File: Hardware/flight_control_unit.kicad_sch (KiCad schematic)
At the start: 43 parts, among them U15 TDD01H0SB1R, U16 TDD01H0SB1R, U7 STM32F405RGT6, Y2 25MHz

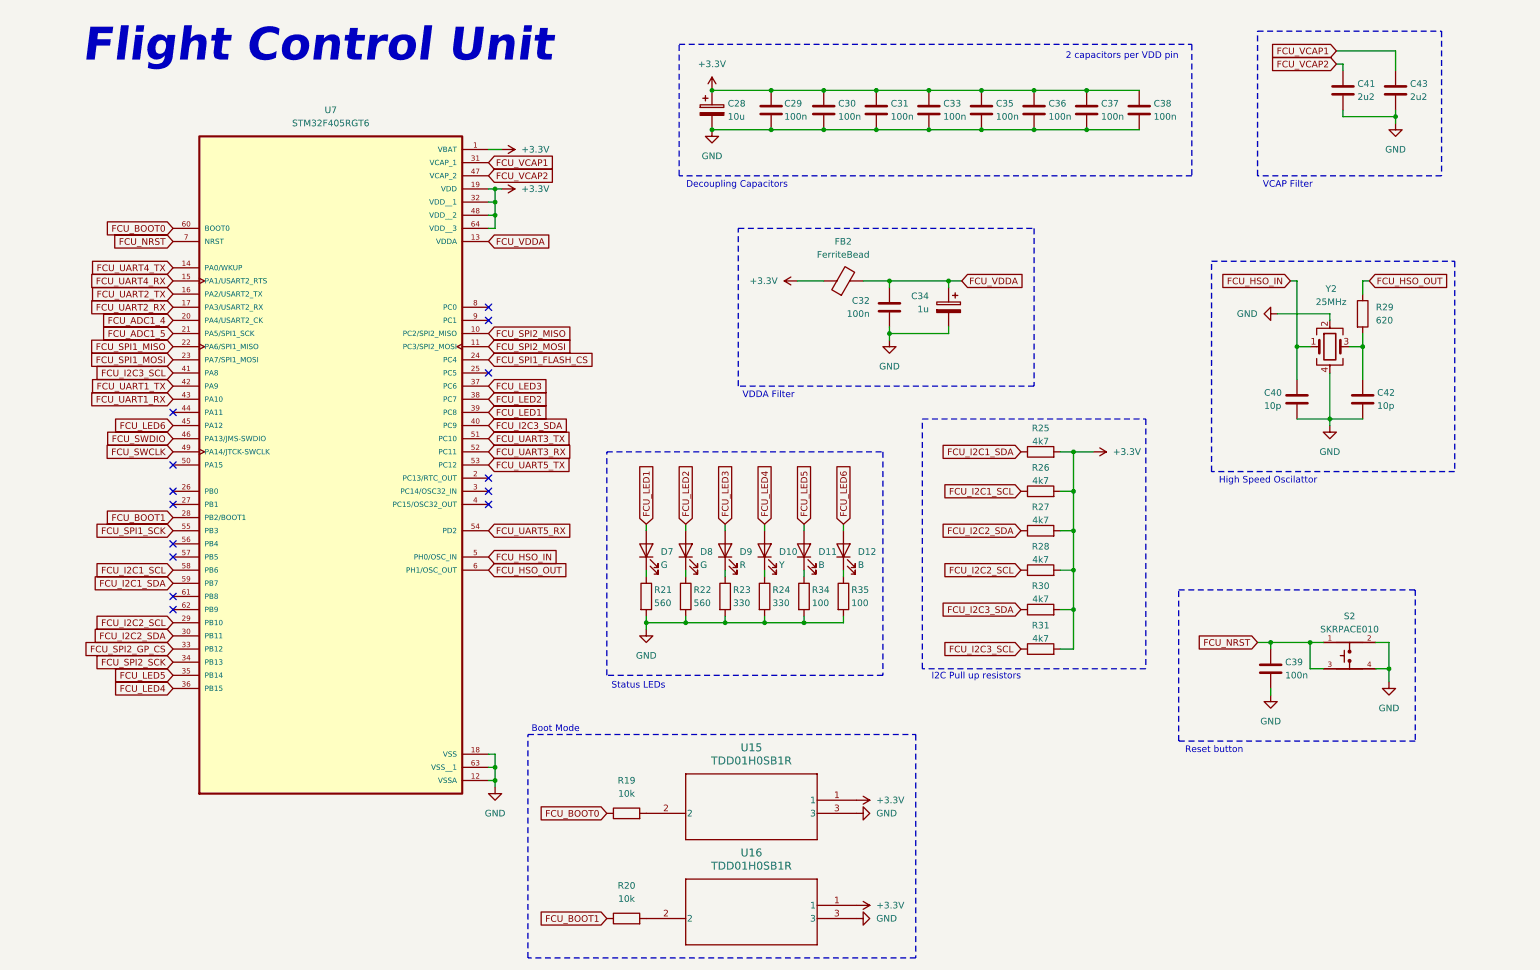
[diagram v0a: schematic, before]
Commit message: fcu, nu schematics, problem with pins
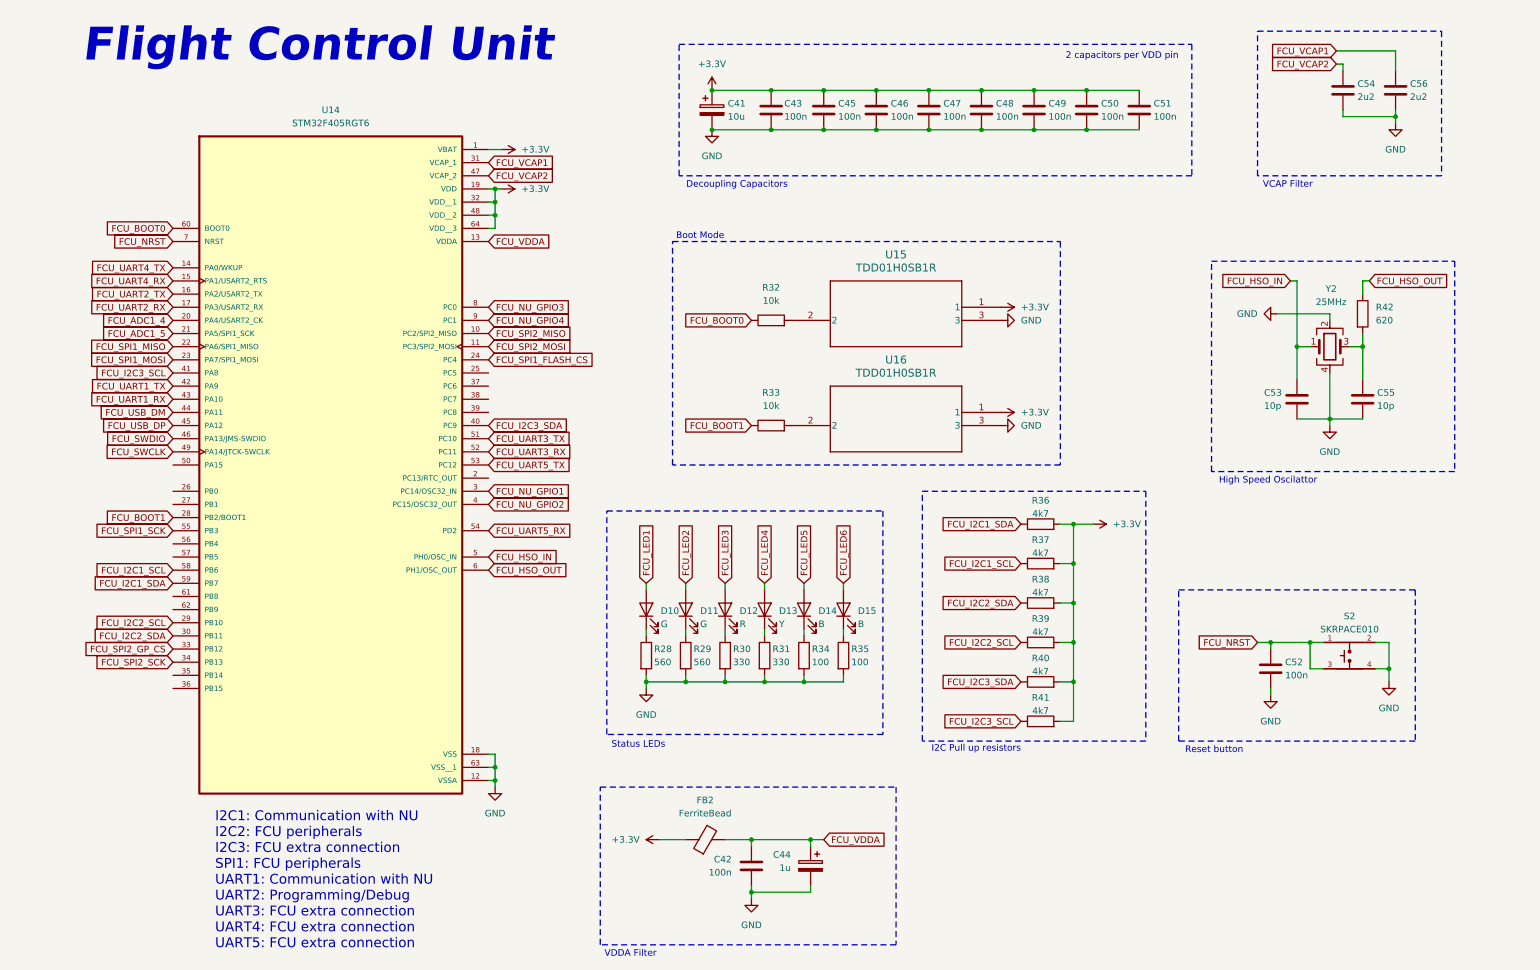
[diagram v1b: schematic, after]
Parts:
- renumbered C28 to C41, C32 to C42, C29 to C43, C34 to C44, C30 to C45, C31 to C46, C33 to C47, C35 to C48, C36 to C49, C37 to C50, C38 to C51, C39 to C52, C40 to C53, C41 to C54, C42 to C55, C43 to C56, D7 to D10, D8 to D11, D9 to D12, D10 to D13, D11 to D14, D12 to D15, R21 to R28, R22 to R29, R23 to R30, R24 to R31, R19 to R32, R20 to R33, R25 to R36, R26 to R37, R27 to R38, R28 to R39, R30 to R40, R31 to R41, R29 to R42, U7 to U14
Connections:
- net FCU_LED1: no longer U14.39 (PC8)
- net FCU_LED2: no longer U14.38 (PC7)
- net FCU_LED3: no longer U14.37 (PC6)
- net FCU_LED4: no longer U14.36 (PB15)
- net FCU_LED5: no longer U14.35 (PB14)
- net FCU_LED6: no longer U14.45 (PA12)
- net FCU_NU_GPIO1: now reaches U14.3 (PC14/OSC32_IN)
- net FCU_NU_GPIO2: now reaches U14.4 (PC15/OSC32_OUT)
- net FCU_USB_DM: now reaches U14.44 (PA11)
- net FCU_NU_GPIO3: now reaches U14.8 (PC0)
- net FCU_NU_GPIO4: now reaches U14.9 (PC1)
- new net FCU_USB_DP: U14.45 (PA12)
- no-connect marks 14 -> 0
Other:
- note added: "I2C1: Communication with NU I2C2: FCU peripherals I2C3: FCU extra connection SPI1: FCU peripherals UART1: Communication with NU UART2: Programming/Debug UART3: FCU extra connection UART4: FCU extra connection UART5: FCU extra connection"
- title: Flight Control Unit - Peripherals -> Flight Control Unit
- moved on the sheet: C42, C44, D10, D11, D12, D13, D14, D15, FB2, R28, R29, R30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

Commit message: pin mess up win, starting over again
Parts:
- removed C41: 10u, symbol Device:C_Polarized
- removed C42, C43, C45, C46, C47, C48, C49, C50, C51, C52: 100n, symbol Device:C
- removed C44: 1u, symbol Device:C_Polarized
- removed C53, C55: 10p, symbol Device:C
- removed C54, C56: 2u2, symbol Device:C
- removed D10, D11: G, symbol Device:LED
- removed D12: R, symbol Device:LED
- removed D13: Y, symbol Device:LED
- removed D14, D15: B, symbol Device:LED
- removed FB2: FerriteBead, symbol Device:FerriteBead
- removed R28, R29: 560, symbol Device:R
- removed R30, R31: 330, symbol Device:R
- removed R32, R33: 10k, symbol Device:R
- removed R34, R35: 100, symbol Device:R
- removed R36, R37, R38, R39, R40, R41: 4k7, symbol Device:R
- removed R42: 620, symbol Device:R
- removed S2: SKRPACE010, SKRPACE010:SW_SKRPACE010, symbol Aircraft_Components:SKRPACE010
- removed U14: STM32F405RGT6, STM32F405RGT6:QFP50P1200X1200X160-64N, symbol Aircraft_Components:STM32F405RGT6
- removed U15, U16: TDD01H0SB1R, SOT_TDDSB1R_CNK, symbol Aircraft_Components:TDD01H0SB1R
- removed Y2: 25MHz, symbol Device:Crystal_GND24
- added C12, C13: 2u2, symbol Device:C
- added C14: 10u, symbol Device:C_Polarized
- added C15, C16, C17, C18, C19, C20, C22, C25, C26: 100n, symbol Device:C
- added C21: 1u, symbol Device:C_Polarized
- added C23, C24: 10p, symbol Device:C
- added D4: R, symbol Device:LED
- added D5: G, symbol Device:LED
- added D6: Y, symbol Device:LED
- added D7: B, symbol Device:LED
- added FB1: FerriteBead, symbol Device:FerriteBead
- added R10: 10k, symbol Device:R
- added R11, R12, R13, R14, R15, R16: 4k7, symbol Device:R
- added R17, R18, R19: 330, symbol Device:R
- added R20: 560, symbol Device:R
- added R9: 620, symbol Device:R
- added SW1: SW_Push_Dual, symbol Switch:SW_Push_Dual
- added SW2: SW_SPDT, symbol Switch:SW_SPDT
- added U14: STM32F405RGTx, Package_QFP:LQFP-64_10x10mm_P0.5mm, symbol MCU_ST_STM32F4:STM32F405RGTx
- added Y1: 25MHz, symbol Device:Crystal_GND24
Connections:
- net +3.3V: now also C14.1, C15.1, C16.1, C17.1, C18.1, C19.1, C25.1, C26.1, FB1.1, R11.1, R12.1, R13.1, R14.1, R15.1, R16.1, SW2.1 (A), U14.1 (VBAT), U14.19 (VDD), U14.32 (VDD), U14.48 (VDD), U14.64 (VDD)
- net FCU_BOOT0: now also R10.1, U14.60 (BOOT0)
- net FCU_I2C1_SCL: now also R11.2, U14.61 (PB8)
- net FCU_I2C1_SDA: now also R12.2, U14.59 (PB7)
- net FCU_I2C2_SCL: now also R13.2, U14.29 (PB10)
- net FCU_I2C2_SDA: now also R14.2, U14.30 (PB11)
- net FCU_I2C3_SCL: now also R15.2, U14.41 (PA8)
- net FCU_I2C3_SDA: now also R16.2, U14.40 (PC9)
- net FCU_LED1: now also D7.2 (A), U14.8 (PC0)
- net FCU_LED2: now also D6.2 (A), U14.9 (PC1)
- net FCU_LED3: now also D5.2 (A), U14.10 (PC2)
- net FCU_LED4: now also D4.2 (A), U14.11 (PC3)
- net FCU_NRST: now also C22.1, SW1.2, SW1.4, U14.7 (NRST)
- net FCU_SPI1_MISO: now also U14.22 (PA6)
- net FCU_SPI1_MOSI: now also U14.23 (PA7)
- net FCU_SWCLK: now also U14.49 (PA14)
- net FCU_SWDIO: now also U14.46 (PA13)
- net FCU_UART1_RX: now also U14.43 (PA10)
- net FCU_UART1_TX: now also U14.42 (PA9)
- net FCU_UART2_RX: now also U14.17 (PA3)
- net FCU_UART2_TX: now also U14.16 (PA2)
- net FCU_UART3_RX: now also U14.52 (PC11)
- net FCU_UART3_TX: now also U14.51 (PC10)
- net FCU_UART4_RX: now also U14.15 (PA1)
- net FCU_UART4_TX: now also U14.14 (PA0)
- net FCU_VDDA: now also C20.1, C21.1, FB1.2, U14.13 (VDDA)
- net GND: now also C12.2, C13.2, C14.2, C15.2, C16.2, C17.2, C18.2, C19.2, C20.2, C21.2, C22.2, C23.2, C24.2, C25.2, C26.2, R17.2, R18.2, R19.2, R20.2, SW1.1, SW1.3, SW2.3 (C), U14.12 (VSSA), U14.18 (VSS), U14.63 (VSS), Y1.2, Y1.4
- new net: D7.1 (K), R20.1
- new net: R10.2, SW2.2 (B)
- new net: D6.1 (K), R19.1
- new net: D4.1 (K), R17.1
- new net: D5.1 (K), R18.1
- new net: C23.1, R9.1, Y1.3
- new net: C12.1, U14.47 (VCAP_2)
- new net: C13.1, U14.31 (VCAP_1)
- new net FCU_NU_GPIOA: U14.38 (PC7)
- new net FCU_NU_GPIOB: U14.37 (PC6)
- new net FCU_NU_GPIOC: U14.36 (PB15)
- new net FCU_NU_GPIOD: U14.35 (PB14)
- new net FCU_NU_GPIOE: U14.34 (PB13)
- new net FCU_NU_GPIOF: U14.33 (PB12)
- new net FCU_OSC_IN: C24.1, U14.5 (PH0), Y1.1
- new net FCU_OSC_OUT: R9.2, U14.6 (PH1)
- new net FCU_SDIO_CLK: U14.53 (PC12)
- new net FCU_SDIO_CMD: U14.54 (PD2)
- new net FCU_SDIO_D0: U14.39 (PC8)
- new net FCU_SP1_FLASH_CS: U14.24 (PC4)
- new net FCU_SPI1_CSK: U14.21 (PA5)
- no-connect marks 0 -> 16
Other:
- note added: "AN4488 - Getting started with STM32F4xxxx MCU hardware development AN2606 - Introduction to system memory boot mode on STM32 MCUs AN2867 - Guidelines for oscillator design on STM8AF/AL/S and STM32 MCUs/MPUs"
- note added: "Boot Mode Selector"
- note added: "High Speed External Crystal (HSE)"
- note added: "I2C Pull-ups"
- note added: "Indicator LEDs"
- note added: "Reset Push Button"
- note removed: "2 capacitors per VDD pin"
- note removed: "Boot Mode"
- note removed: "Flight Control Unit"
- note removed: "High Speed Oscilattor"
- note removed: "I2C Pull up resistors"
- note removed: "I2C1: Communication with NU I2C2: FCU peripherals I2C3: FCU extra connection SPI1: FCU peripherals UART1: Communication with NU UART2: Programming/Debug UART3: FCU extra connection UART4: FCU extra connection UART5: FCU extra connection"
- note removed: "Reset button"
- note removed: "Status LEDs"
- note removed: "VCAP Filter"

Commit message: added projects, schematic almost done, need revision
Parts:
- renumbered C13 to C25, C12 to C26, C14 to C27, C24 to C28, C15 to C29, C16 to C30, C23 to C31, C17 to C32, C18 to C33, C19 to C34, C25 to C35, C26 to C36, C20 to C37, C22 to C38, C21 to C39, R17 to R13, R9 to R14, R10 to R15, R18 to R16, R19 to R17, R20 to R18, R11 to R19, R12 to R20, R13 to R21, R14 to R22, R15 to R23, R16 to R24, SW2 to SW1, SW1 to SW2, U14 to U12
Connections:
- net FCU_NU_GPIOC is gone; now on net FCU_LED1: U12.36 (PB15)
- net FCU_NU_GPIOD is gone; now on net FCU_LED2: U12.35 (PB14)
- net FCU_NU_GPIOE is gone; now on net FCU_LED3: U12.34 (PB13)
- net FCU_NU_GPIOF is gone; now on net FCU_LED4: U12.33 (PB12)
- net FCU_I2C1_SDA: now also U12.62 (PB9); no longer U12.59 (PB7)
- net FCU_I2C3_SCL: no longer U12.41 (PA8)
- net FCU_I2C3_SDA: no longer U12.40 (PC9)
- net FCU_LED1: no longer U12.8 (PC0)
- net FCU_LED2: no longer U12.9 (PC1)
- net FCU_LED3: no longer U12.10 (PC2)
- net FCU_LED4: no longer U12.11 (PC3)
- net FCU_UART1_RX: now also U12.59 (PB7); no longer U12.43 (PA10)
- net FCU_UART1_TX: now also U12.58 (PB6); no longer U12.42 (PA9)
- net FCU_GPIOG: now reaches U12.2 (PC13)
- net FCU_TIM3_RUDD: now reaches U12.26 (PB0)
- net FCU_TIM3_FLAP: now reaches U12.27 (PB1)
- net FCU_GPIOF: now reaches U12.3 (PC14)
- net FCU_GPIOE: now reaches U12.4 (PC15)
- net FCU_SDIO_DET: now reaches U12.55 (PB3)
- net FCU_NU_GPIOA renamed FCU_TIM3_ELEV
- net FCU_NU_GPIOB renamed FCU_TIM3_ALRN
- new net FCU_GPIOA: U12.11 (PC3)
- new net FCU_GPIOB: U12.10 (PC2)
- new net FCU_GPIOC: U12.9 (PC1)
- new net FCU_GPIOD: U12.8 (PC0)
- new net FCU_TIM1_ESC1: U12.42 (PA9)
- new net FCU_TIM1_ESC2: U12.43 (PA10)
- no-connect marks 16 -> 10
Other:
- note added: "Flight Control Unit"
- moved on the sheet: C27, C29, C30, C32, C33, C34, C35, C36

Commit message: version 0.1.0
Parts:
- renumbered C25 to C40, C26 to C41, C27 to C42, C28 to C43, C29 to C44, C30 to C45, C31 to C46, C32 to C47, C33 to C48, C34 to C49, C35 to C50, C36 to C51, C37 to C52, C38 to C53, C39 to C54, D6 to D10, D7 to D11, D4 to D8, D5 to D9, FB1 to FB2, R13 to R25, R14 to R26, R15 to R27, R16 to R28, R17 to R29, R18 to R30, R19 to R31, R20 to R32, R21 to R33, R22 to R34, R23 to R35, R24 to R36, SW1 to SW3, SW2 to SW4, Y1 to Y2

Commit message: version 0.1.1, added dfu usb to firmware upload, changed pwm channels
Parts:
- removed R35, R36: 4k7, symbol Device:R
- added TP1, TP2: I2C1, symbol Connector:TestPoint
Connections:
- net FCU_I2C1_SCL: now also TP2.1
- net FCU_I2C1_SDA: now also TP1.1
- net FCU_TIM1_CH1: now reaches U12.41 (PA8)
- net FCU_USB_OTG_FS_DM: now reaches U12.44 (PA11)
- net FCU_USB_OTG_FS_DP: now reaches U12.45 (PA12)
- net FCU_SPI1_CSK renamed FCU_SPI1_SCK
- net FCU_TIM1_ESC1 renamed FCU_USB_OTG_FS_VBUS
- net FCU_TIM1_ESC2 renamed FCU_TIM1_CH3
- net FCU_TIM3_ALRN renamed FCU_TIM3_CH1
- net FCU_TIM3_ELEV renamed FCU_TIM3_CH2
- net FCU_TIM3_FLAP renamed FCU_TIM3_CH4
- net FCU_TIM3_RUDD renamed FCU_TIM3_CH3
- no-connect marks 10 -> 7
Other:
- note added: "I2C1 Test Point"
